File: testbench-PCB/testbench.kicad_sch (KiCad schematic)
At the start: 0 parts

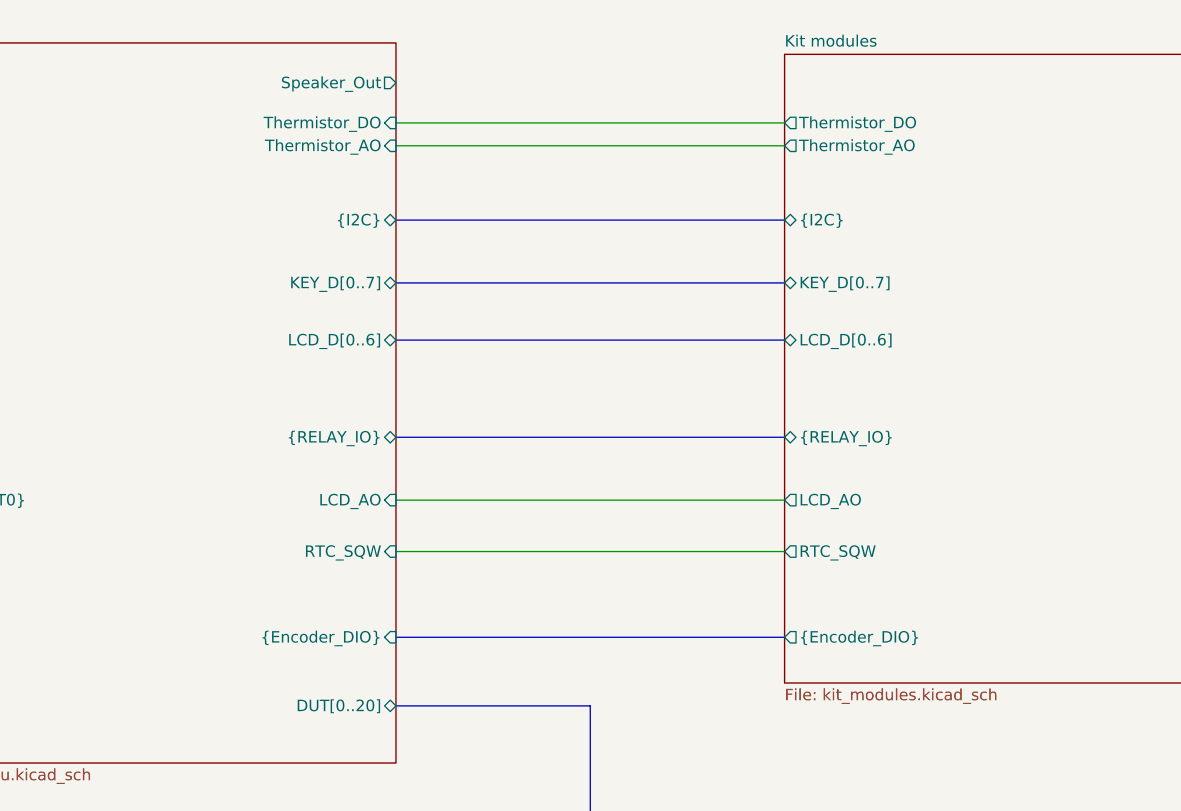
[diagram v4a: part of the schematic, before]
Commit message: Connecter speaker, added JTAG.
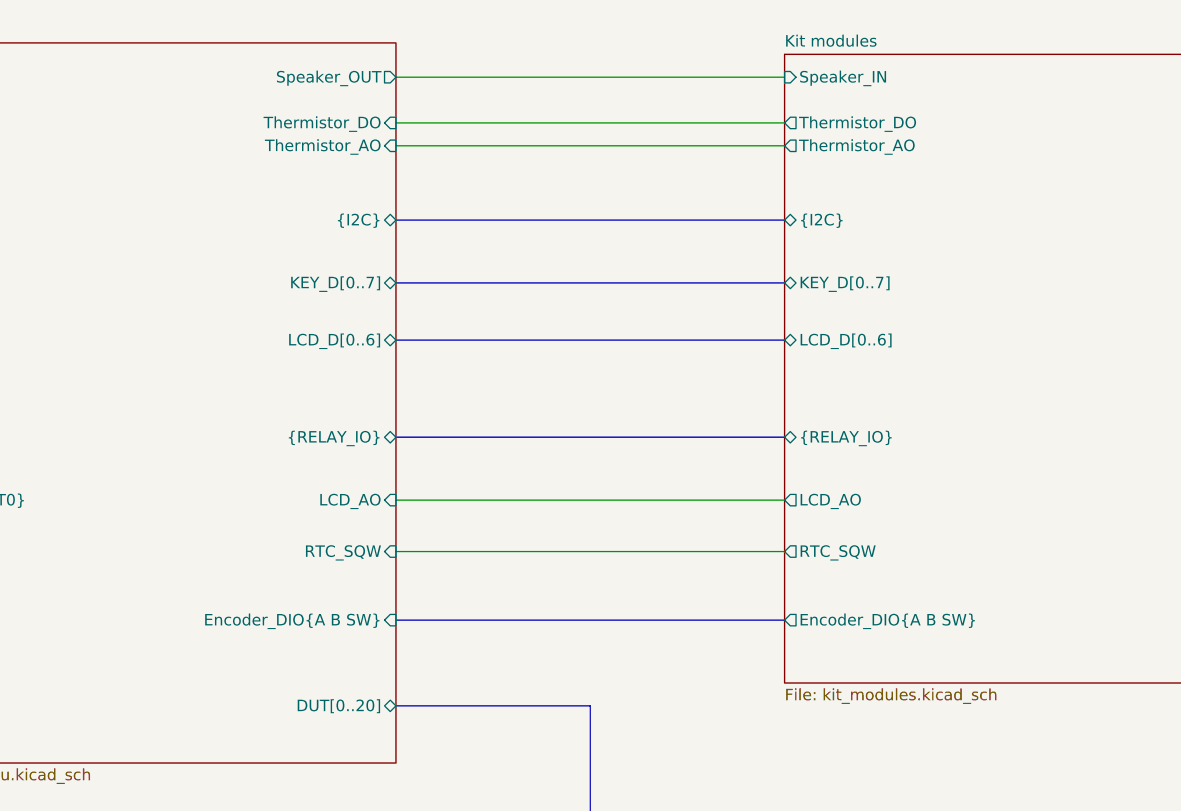
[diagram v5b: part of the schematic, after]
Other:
- sheet Kit modules ports: added Encoder_DIO{A B SW}, Speaker_IN; removed {Encoder_DIO}
- sheet MCU ports: added Encoder_DIO{A B SW}, Speaker_OUT; removed Speaker_Out, {Encoder_DIO}
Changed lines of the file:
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@@
+    (stroke (width 0) (type default))
+  )
+  (bus (pts (xy 148.59 88.265) (xy 191.77 88.265))
     (stroke (width 0) (type default))
   )
@@
     (stroke (width 0) (type default))
   )
+  (wire (pts (xy 148.59 27.94) (xy 191.77 27.94))
+    (stroke (width 0) (type default))
+  )
   (bus (pts (xy 148.59 67.945) (xy 191.77 67.945))
     (stroke (width 0) (type default))
   )
   (bus (pts (xy 148.59 57.15) (xy 191.77 57.15))
-    (stroke (width 0) (type default))
-  )
-  (bus (pts (xy 191.77 90.17) (xy 148.59 90.17))
     (stroke (width 0) (type default))
   )
@@
       (effects (font (size 1.27 1.27)) (justify right))
     )
-    (pin "Speaker_Out" output (at 148.59 28.575 0)
-      (effects (font (size 1.27 1.27)) (justify right))
-    )
     (pin "{RELAY_IO}" bidirectional (at 148.59 67.945 0)
       (effects (font (size 1.27 1.27)) (justify right))
@@
       (effects (font (size 1.27 1.27)) (justify right))
     )
-    (pin "{Encoder_DIO}" input (at 148.59 90.17 0)
-      (effects (font (size 1.27 1.27)) (justify right))
-    )
     (pin "Thermistor_DO" input (at 148.59 33.02 0)
       (effects (font (size 1.27 1.27)) (justify right))
@@
     )
     (pin "LCD_AO" input (at 148.59 74.93 0)
+      (effects (font (size 1.27 1.27)) (justify right))
+    )
+    (pin "Encoder_DIO{A B SW}" input (at 148.59 88.265 0)
+      (effects (font (size 1.27 1.27)) (justify right))
+    )
+    (pin "Speaker_OUT" output (at 148.59 27.94 0)
       (effects (font (size 1.27 1.27)) (justify right))
     )
@@
       (effects (font (size 1.27 1.27)) (justify left))
     )
-    (pin "{Encoder_DIO}" output (at 191.77 90.17 180)
-      (effects (font (size 1.27 1.27)) (justify left))
-    )
     (pin "{I2C}" bidirectional (at 191.77 43.815 180)
       (effects (font (size 1.27 1.27)) (justify left))
@@
       (effects (font (size 1.27 1.27)) (justify left))
     )
+    (pin "Encoder_DIO{A B SW}" output (at 191.77 88.265 180)
+      (effects (font (size 1.27 1.27)) (justify left))
+    )
+    (pin "Speaker_IN" input (at 191.77 27.94 180)
+      (effects (font (size 1.27 1.27)) (justify left))
+    )

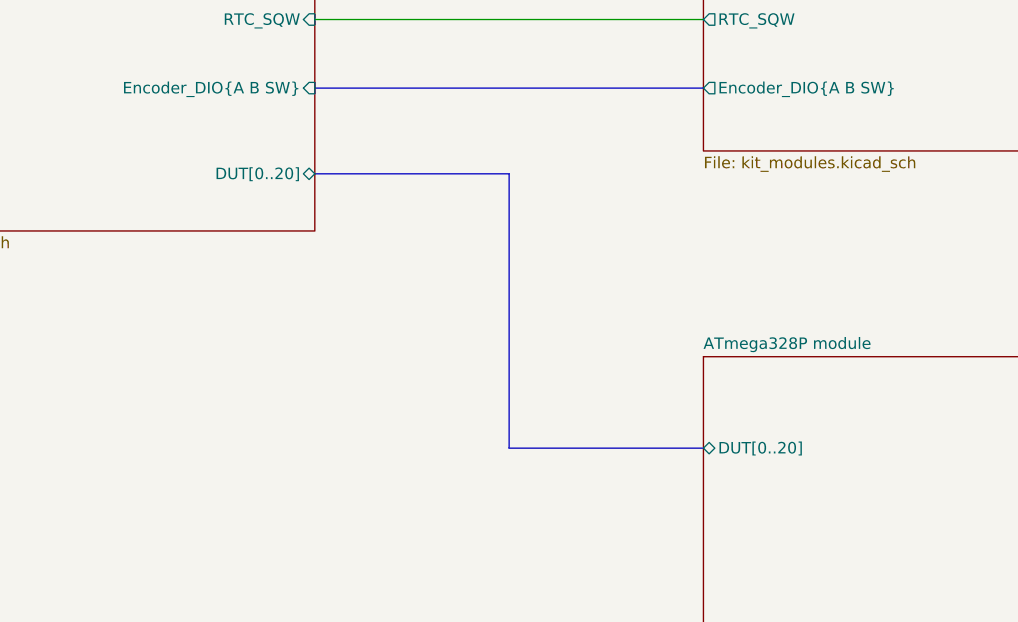
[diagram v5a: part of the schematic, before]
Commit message: Rearanged PCB, updated footprints.
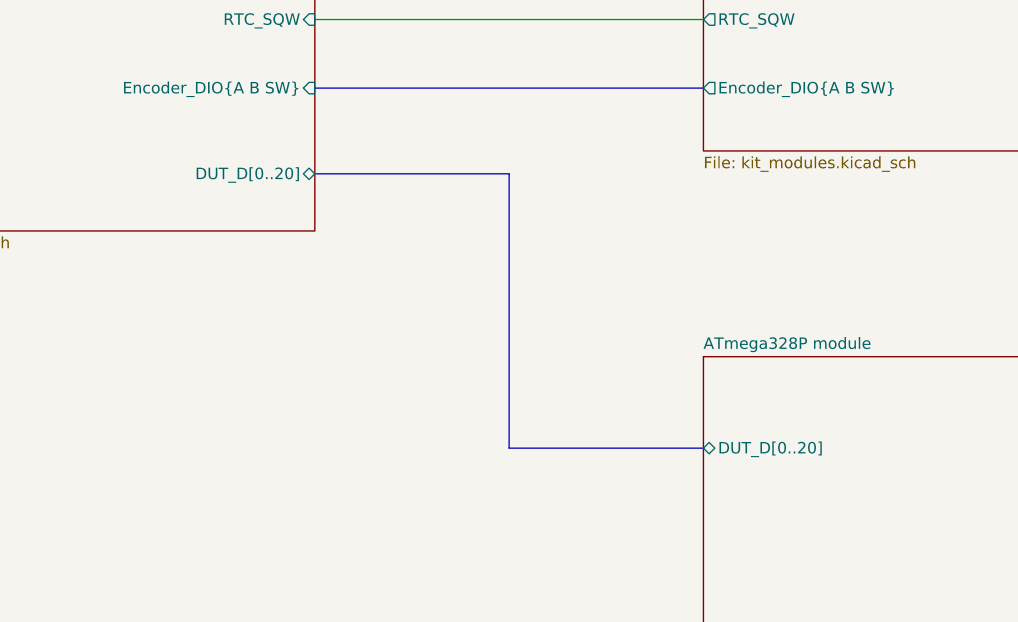
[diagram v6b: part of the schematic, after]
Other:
- sheet ATmega328P module ports: added DUT_D[0..20]; removed DUT[0..20]
- sheet MCU ports: added DUT_D[0..20]; removed DUT[0..20]
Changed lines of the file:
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@@
+    (stroke (width 0) (type default))
+  )
+  (bus (pts (xy 170.18 128.27) (xy 191.77 128.27))
     (stroke (width 0) (type default))
   )
@@
   )
   (bus (pts (xy 148.59 88.265) (xy 191.77 88.265))
-    (stroke (width 0) (type default))
-  )
-  (bus (pts (xy 170.18 128.27) (xy 191.77 128.27))
     (stroke (width 0) (type default))
   )
@@
       (effects (font (size 1.27 1.27)) (justify right))
     )
-    (pin "DUT[0..20]" bidirectional (at 148.59 97.79 0)
-      (effects (font (size 1.27 1.27)) (justify right))
-    )
     (pin "Thermistor_DO" input (at 148.59 33.02 0)
       (effects (font (size 1.27 1.27)) (justify right))
@@
     )
     (pin "Speaker_OUT" output (at 148.59 27.94 0)
+      (effects (font (size 1.27 1.27)) (justify right))
+    )
+    (pin "DUT_D[0..20]" bidirectional (at 148.59 97.79 0)
       (effects (font (size 1.27 1.27)) (justify right))
     )
@@
       (effects (font (size 1.27 1.27)) (justify left top))
     )
-    (pin "DUT[0..20]" bidirectional (at 191.77 128.27 180)
+    (pin "DUT_D[0..20]" bidirectional (at 191.77 128.27 180)
       (effects (font (size 1.27 1.27)) (justify left))
     )
